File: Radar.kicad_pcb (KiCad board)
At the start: 4 copper layers, 76.4 x 74 mm, 113 parts, among them J1 Receive_Antenna, J10 Conn_Coaxial, J11 Conn_02x05_Odd_Even, J12 Conn_02x03_Odd_Even, J13 RF_Shield_Two_Pieces, J2 VCO_Tune, J3 Transmit Antenna, J4 Output, J5 Conn_Coaxial, J6 Conn_Coaxial, J7 Conn_Coaxial, J8 Conn_Coaxial, J9 Conn_Coaxial, U10 AD5252, U11 LT1722, U12 AD8039, U13 PMA-63GLN+, U14 QPC6324, U15 PMA-63GLN+, U16 QPC6324, U17 HMC218BMS8GE, U18 AZ1117-5.0, U19 RP117, U20 MIC5317, U21 L78L33_SO8, U23 HMC430, U24 RFPA5542

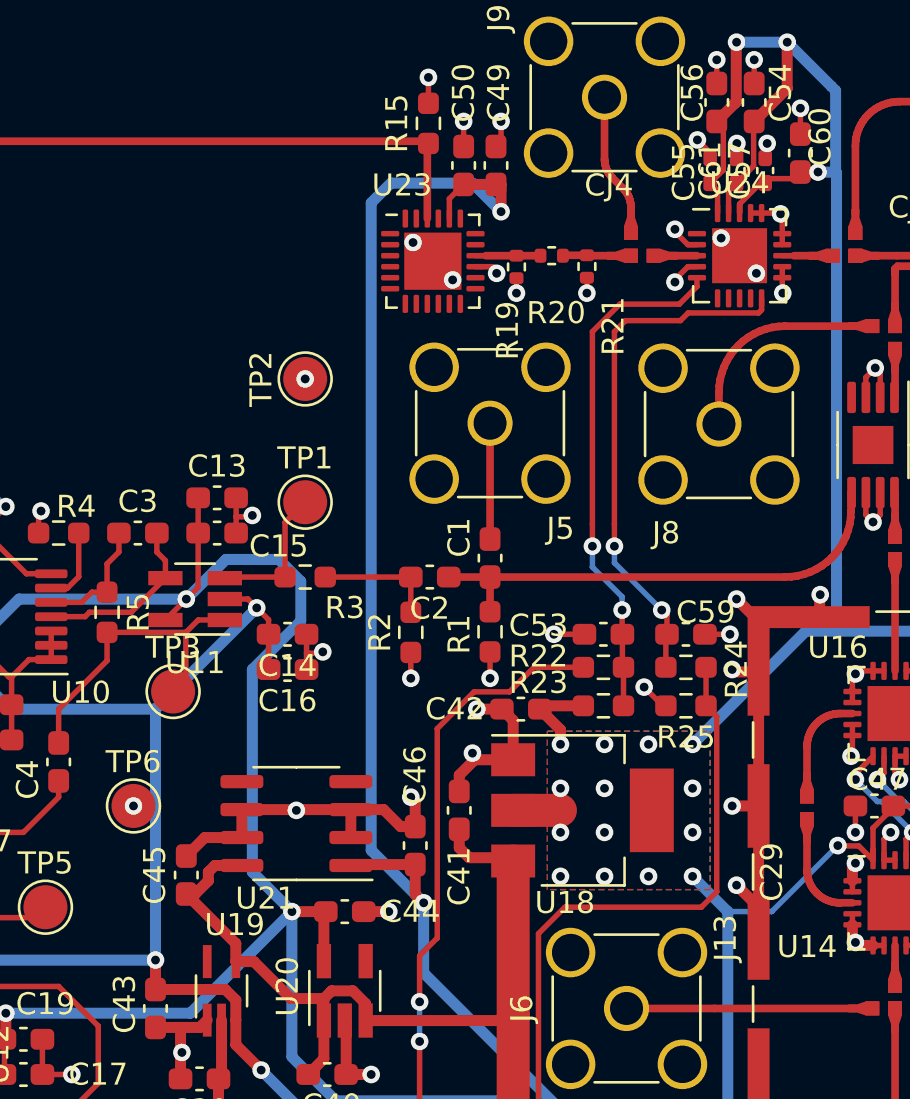
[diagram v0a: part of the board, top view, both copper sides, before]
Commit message: replaced 78xx series 3V3 regulator  for 1117 series
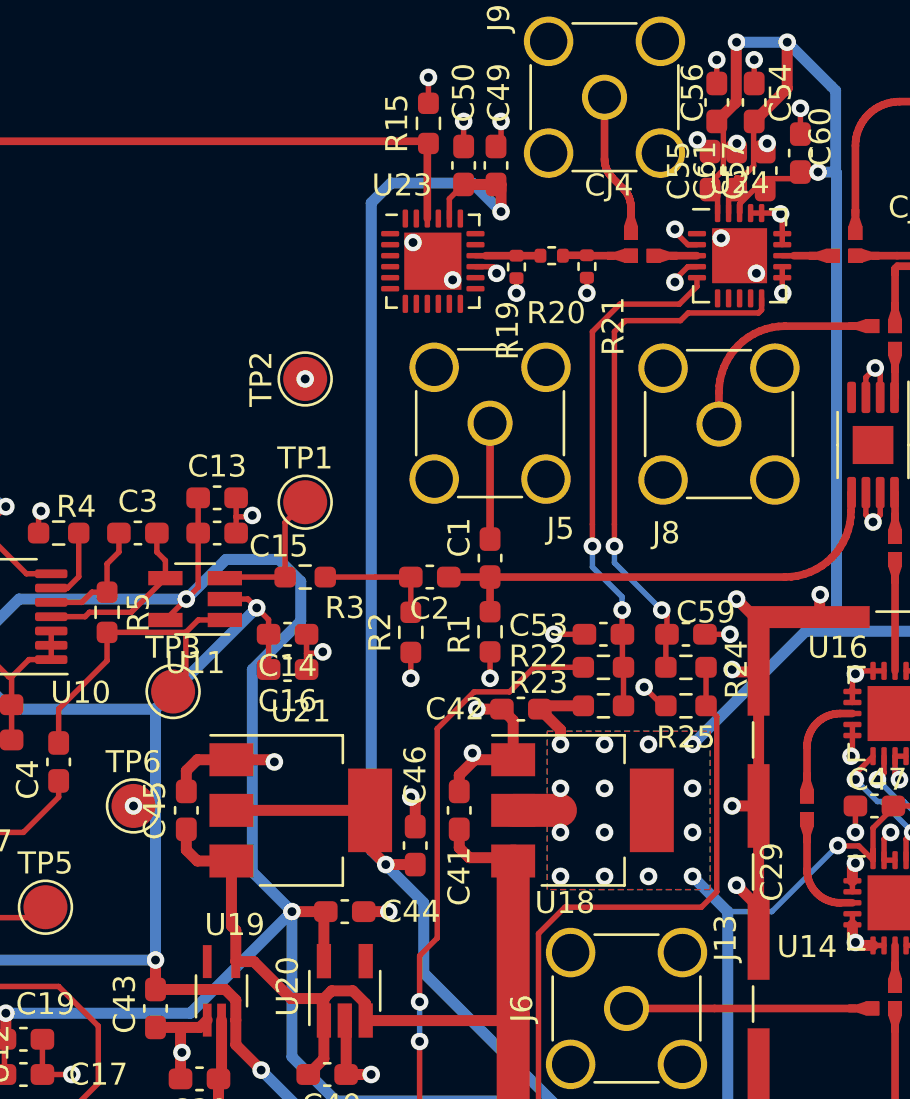
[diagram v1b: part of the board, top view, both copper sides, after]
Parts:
- C45: value 1uF -> 10uF
- C46: value 100nF -> 10uF
- C55, C57, C61: footprint Capacitor_SMD:C_0402_1005Metric_Pad0.74x0.62mm_HandSolder -> Capacitor_SMD:C_0603_1608Metric_Pad1.08x0.95mm_HandSolder
- U21: value L78L33_SO8 -> LT1117-3.3; footprint Package_SO:SOIC-8_3.9x4.9mm_P1.27mm -> Package_TO_SOT_SMD:SOT-223-3_TabPin2
- moved C45 2.94 mm to (129.8, 70.0)
- moved U21 0.63 mm to (135.0, 70.0), turned to 0 degrees
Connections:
- J12 pad 6: (no net) -> Net-(J12-Pad6)
- U21 pad 1: +3V3 -> GND
- U21 pad 2: GND -> +3V3
- U21 pad 3: GND -> +6V
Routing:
- net GND: track 225.9 -> 217.4 mm
- net +3V3: track 67.5 -> 73.0 mm
- net +6V: track 59.9 -> 60.4 mm

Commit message: Added names
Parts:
- C55, C57, C61: footprint Capacitor_SMD:C_0603_1608Metric_Pad1.08x0.95mm_HandSolder -> Resistor_SMD:R_0402_1005Metric_Pad0.72x0.64mm_HandSolder
- moved J1 0.05 mm to (177.9, 84.8)
- moved J3 0.05 mm to (177.9, 44.8)
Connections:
- J12 pad 6: Net-(J12-Pad6) -> (no net)
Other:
- net class RF: clearance 0.15 -> 0.09
- rule trace_min: 0.2 -> 0.1
- board text added: "Jakub Jendryka Jan Sobków Szymon Zakrent"

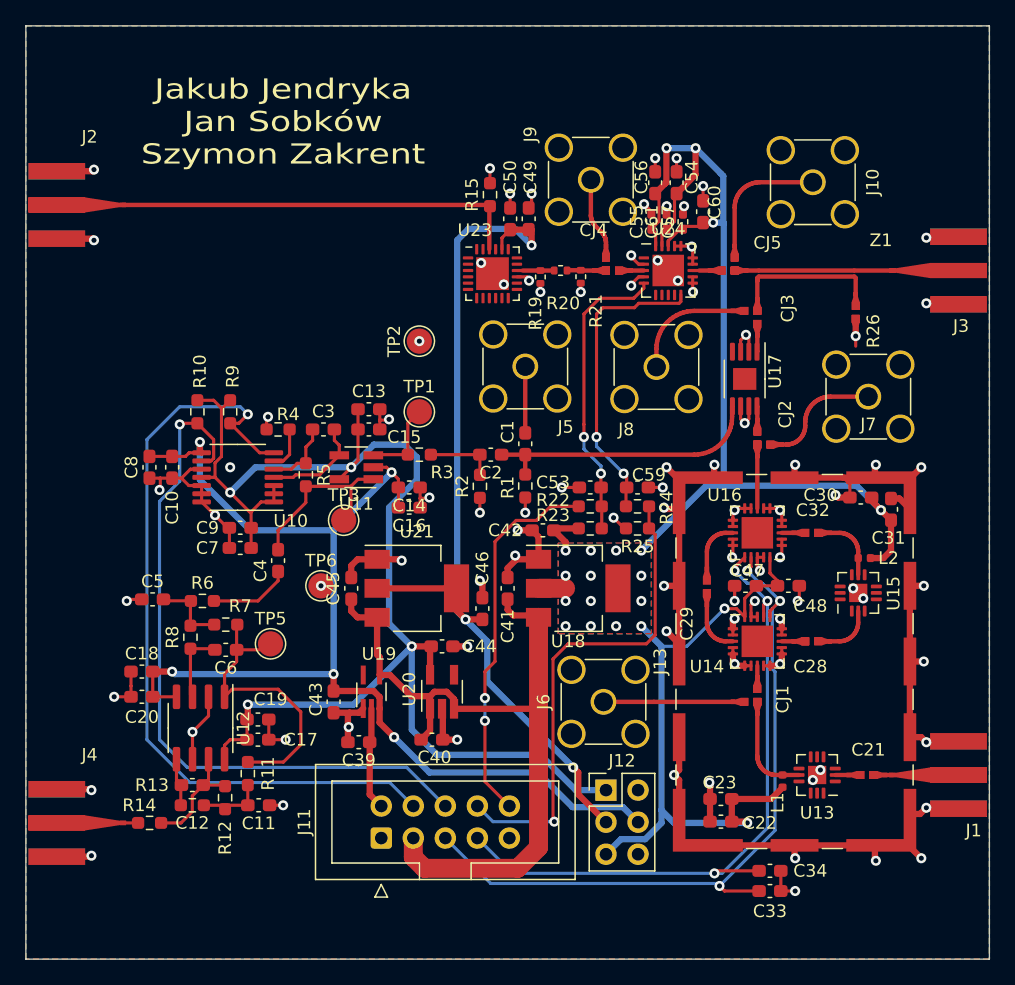
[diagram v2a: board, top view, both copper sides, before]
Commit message: Added via stitching
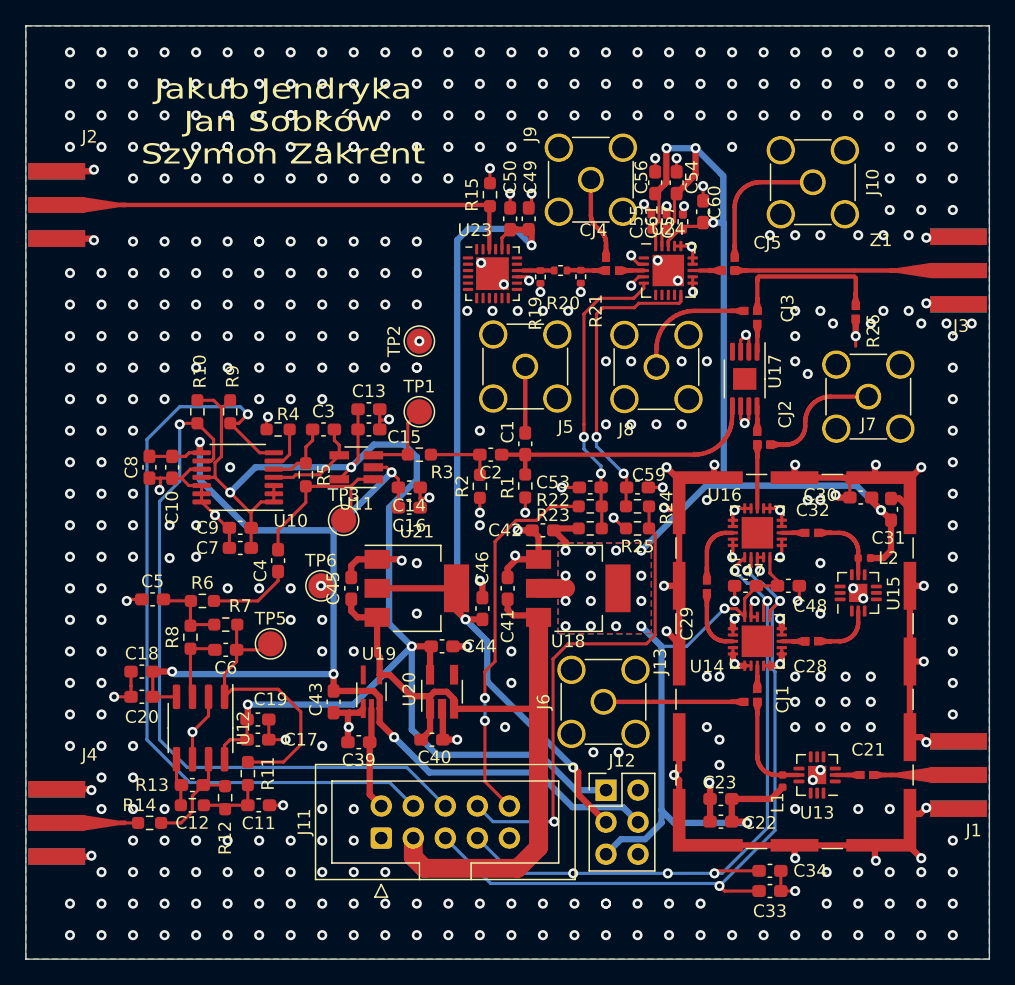
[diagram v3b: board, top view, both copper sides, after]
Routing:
- net GND: vias 89 -> 485
- net /Connector/SW_CTR1: vias 3 -> 5

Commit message: Added pinout
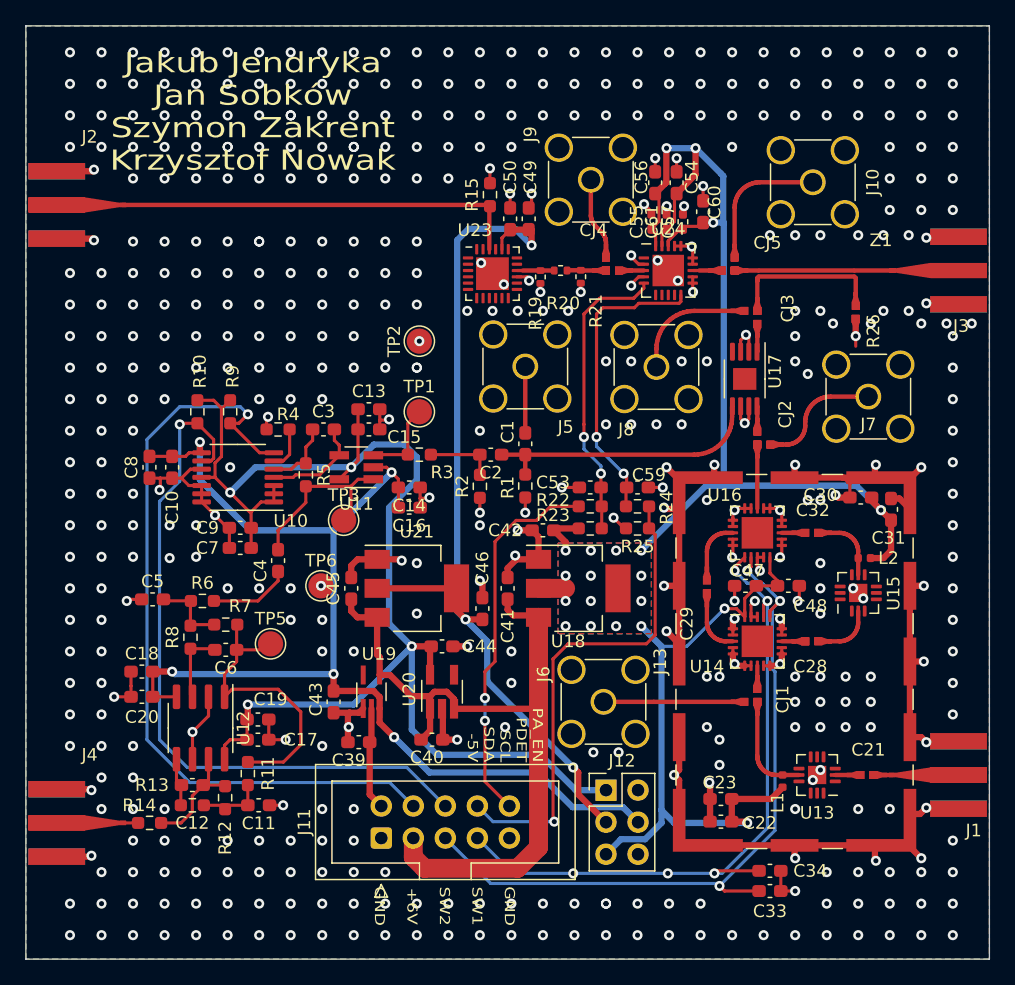
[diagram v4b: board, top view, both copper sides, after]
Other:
- board text added: "GND SW1 SW2 +6V GND"
- board text added: "Jakub Jendryka Jan Sobków Szymon Zakrent Krzysztof Nowak"
- board text added: "PA_EN PDET SCL SDA -5V"
- board text removed: "Jakub Jendryka Jan Sobków Szymon Zakrent"
